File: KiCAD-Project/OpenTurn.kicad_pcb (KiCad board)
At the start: 4 copper layers, 66 x 84.5 mm, 146 parts, among them J201 XT30, J202 Conn_02x04_Odd_Even, J203 Conn_01x03_Shielded, J204 Conn_01x03_Shielded, J301 GPIOs, J302 JTAG/SWD, J303 Conn_01x03_Shielded, Q501 IAUC120N06S5N017ATMA1, Q502 IAUC120N06S5N017ATMA1, Q601 IAUC120N06S5N017ATMA1, Q602 IAUC120N06S5N017ATMA1, Q701 IAUC120N06S5N017ATMA1, Q702 IAUC120N06S5N017ATMA1, U201 TI_TCAN337G, U202 TLE5012B_E1000, U203 MAX15062A, U301 CY8C6244AZI-S4D92, U302 MCP9700AT-HTT, U401 DRV8323SRTAR-DRV8323SRTAR, Y301 32MHz

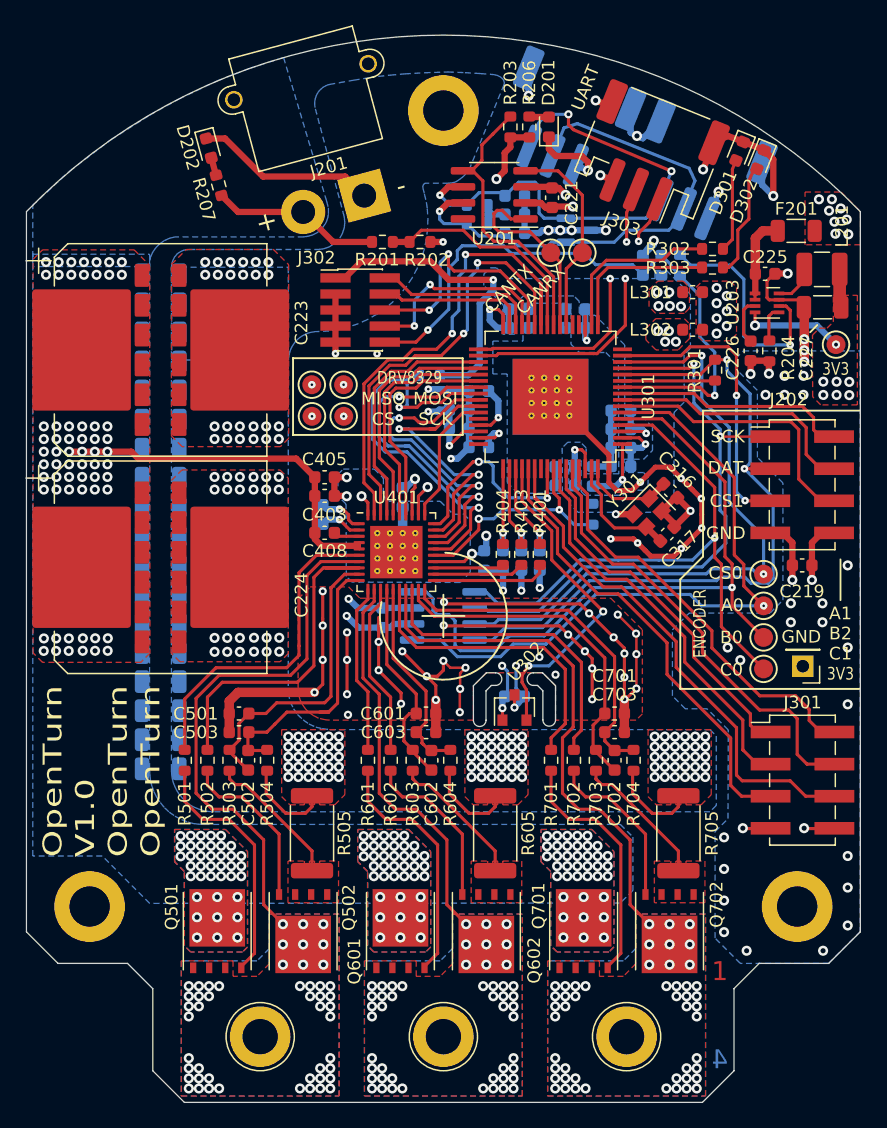
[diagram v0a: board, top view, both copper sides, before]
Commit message: changed connectors to THT
changed connectors to THT, removed UART connector
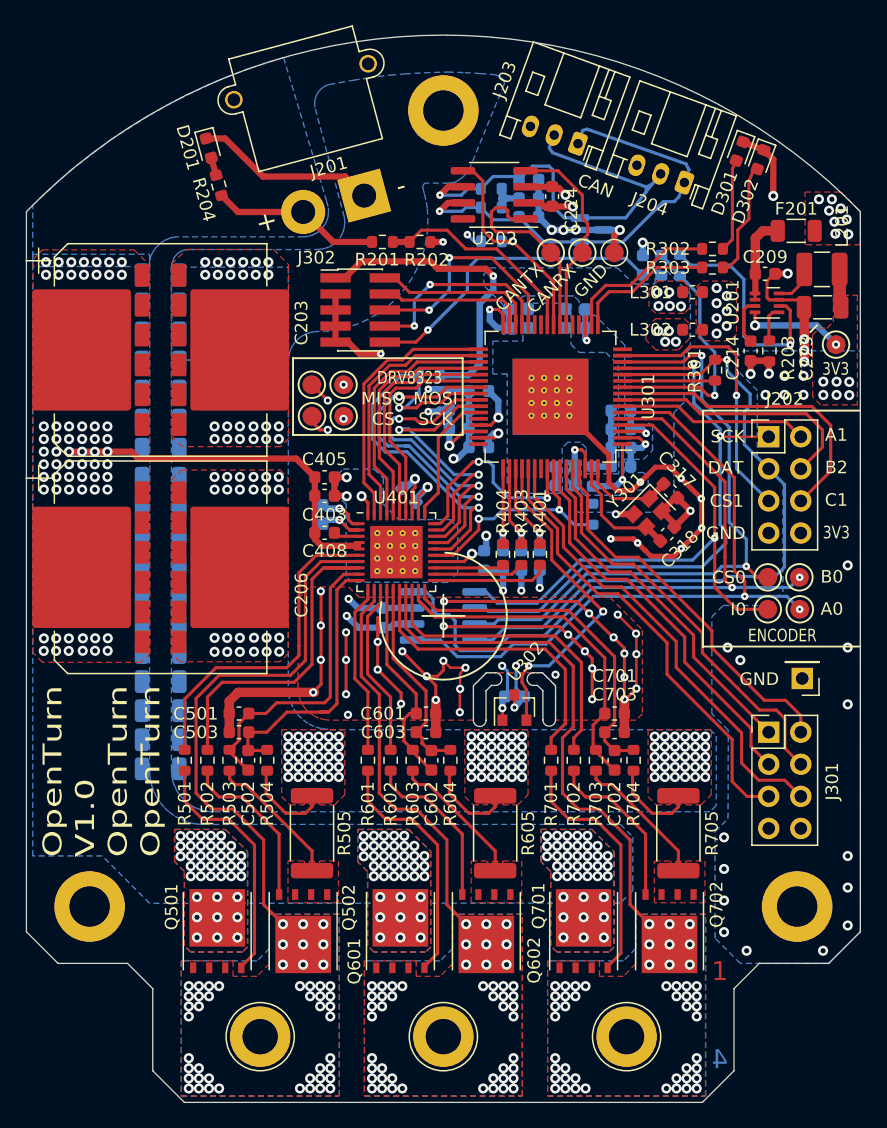
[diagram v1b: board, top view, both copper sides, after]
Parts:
- removed the C219 at (155.4, 123.0)
- removed the D201 at (135.3, 88.3)
- removed J303: Conn_01x03_Shielded, Connector_JST:JST_PH_S3B-PH-SM4-TB_1x03-1MP_P2.00mm_Horizontal
- removed the R206 at (133.8, 88.3)
- added TP203: CAN_GND, TestPoint:TestPoint_Pad_D1.5mm, F.Cu at (140.5, 98.2)
- C225: renamed from C1; value 100n -> 4n7
- J202, J301: footprint Connector_PinHeader_2.54mm:PinHeader_2x04_P2.54mm_Vertical_SMD -> Connector_PinHeader_2.54mm:PinHeader_2x04_P2.54mm_Vertical
- J203, J204: footprint Connector_JST:JST_PH_S3B-PH-SM4-TB_1x03-1MP_P2.00mm_Horizontal -> Connector_JST:JST_PH_S3B-PH-K_1x03_P2.00mm_Horizontal; moved to F.Cu
- R206: renamed from R203; moved to B.Cu
- moved R206 9.17 mm to (130.8, 97.3), turned to 0 degrees
- moved TP206 5.54 mm to (155.2, 123.9)
- moved TP204 4.73 mm to (152.7, 126.5), turned to 90 degrees
- moved J301 4.64 mm to (152.8, 136.2)
- moved J202 4.63 mm to (152.8, 112.8)
- moved TP207 2.88 mm to (155.2, 126.5), turned to 90 degrees
- moved J203 1.93 mm to (137.7, 89.6), turned to 160 degrees
- moved R207 1.69 mm to (130.8, 94.7)
- moved C226 1.69 mm to (133.8, 95.4)
- moved C227 1.69 mm to (133.8, 92.5)
- moved C225 1.69 mm to (133.8, 93.9)
- moved R208 1.69 mm to (130.8, 93.2)
- moved J204 1.16 mm to (146.1, 92.7), turned to 160 degrees
- moved D202 1.11 mm to (138.7, 96.4)
- moved TP302 0.98 mm to (155.4, 131.9)
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- renumbered C223 to C203, C203 to C204, C204 to C205, C224 to C206, C205 to C207, C206 to C208, C225 to C209, C207 to C210, C208 to C211, C209 to C212, C210 to C213, C226 to C214, C211 to C215, C212 to C216, C213 to C217, C214 to C218, C215 to C219, C216 to C220, C217 to C221, C218 to C222, C227 to C223, C221 to C224, C2 to C226, C3 to C227, C222 to C228, C311 to C305, C305 to C306, C322 to C307, C312 to C308, C306 to C309, C307 to C310, C314 to C311, C308 to C312, C309 to C313, C310 to C314, C313 to C315, C315 to C316, C316 to C317, C317 to C318, C318 to C319, D202 to D201, D1 to D202, R204 to R203, R207 to R204, R1 to R207, R2 to R208, R305 to R304, TP202 to TP201, TP203 to TP202, TP206 to TP204, TP204 to TP205, TP205 to TP206, TP201 to TP207, U203 to U201, U201 to U202, U202 to U203
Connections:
- C226 pad 1: Net-(C2-Pad1) -> Net-(C226-Pad1)
- C227 pad 1: Net-(C3-Pad1) -> Net-(C227-Pad1)
- D202 pad 1: Net-(C2-Pad1) -> Net-(C226-Pad1)
- D202 pad 2: Net-(C3-Pad1) -> Net-(C227-Pad1)
- H101 pad 1: GND -> unconnected-(H101-Pad1)
- H102 pad 1: GND -> unconnected-(H102-Pad1)
- J202 pad 2: /Interfaces/ENCODER_QOAD_I2 -> /Interfaces/ENCODER_QOAD_A2
- J202 pad 6: /Interfaces/ENCODER_QOAD_A2 -> /Interfaces/ENCODER_QOAD_I2
- J202 pad 7: GND -> +3V3
- J202 pad 8: +3V3 -> GND
- J203 pad 1: Net-(C3-Pad1) -> Net-(C226-Pad1)
- J203 pad 2: Net-(C2-Pad1) -> Net-(C227-Pad1)
- J204 pad 1: Net-(C3-Pad1) -> Net-(C226-Pad1)
- J204 pad 2: Net-(C2-Pad1) -> Net-(C227-Pad1)
- R207 pad 1: Net-(C2-Pad1) -> Net-(C226-Pad1)
- R208 pad 1: Net-(C3-Pad1) -> Net-(C227-Pad1)
- U202 pad 6: Net-(C3-Pad1) -> Net-(C227-Pad1)
- U202 pad 7: Net-(C2-Pad1) -> Net-(C226-Pad1)
- U301 pad 26: /MCU/DRV_PWM_AL -> unconnected-(U301-Pad26)
- U301 pad 27: /MCU/DRV_PWM_AH -> unconnected-(U301-Pad27)
- U301 pad 33: /MCU/DEBUG_UART_RX -> /MCU/DRV_PWM_AL
- U301 pad 34: /MCU/DEBUG_UART_TX -> /MCU/DRV_PWM_AH
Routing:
- net Net-(C2-Pad1): track 41.1 -> 0.00 mm, vias 1 -> 0
- net Net-(C3-Pad1): track 40.9 -> 0.00 mm, vias 3 -> 0
- net Net-(C226-Pad1): track 0.00 -> 36.6 mm, vias 0 -> 1
- net Net-(C227-Pad1): track 0.00 -> 36.1 mm, vias 0 -> 1
- net GND: track 307.9 -> 276.5 mm, vias 242 -> 227
- net /MCU/DEBUG_UART_TX: track 23.6 -> 0.00 mm, vias 2 -> 0
- net /MCU/DEBUG_UART_RX: track 22.9 -> 0.00 mm, vias 2 -> 0
- net /MCU/DRV_PWM_AL: track 39.4 -> 20.9 mm, vias 2 -> 0
- net /MCU/DRV_PWM_AH: track 33.9 -> 20.3 mm, vias 2 -> 0
- net +3V3: track 65.2 -> 56.8 mm, vias 20 -> 18
- net /Interfaces/ENCODER_QOAD_A2: track 22.1 -> 15.1 mm
- net /Interfaces/ENCODER_QOAD_I2: track 18.7 -> 24.5 mm
- net /Interfaces/CANFD_Fault: track 23.7 -> 18.1 mm, vias 0 -> 1
- net /MCU/GPIO5: track 41.0 -> 37.6 mm
- net /Interfaces/ENCODER_QOAD_I1: track 46.8 -> 43.8 mm
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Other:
- board text added: "48V 15A"
- board text added: "DRV8323"
- board text added: "I0"
- board text removed: "48V 20A"
- board text removed: "C0"
- board text removed: "DRV8329"
- board text removed: "UART"

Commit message: minor pcb updates
swapped Encoder Quadrature signals, to provide debug UART
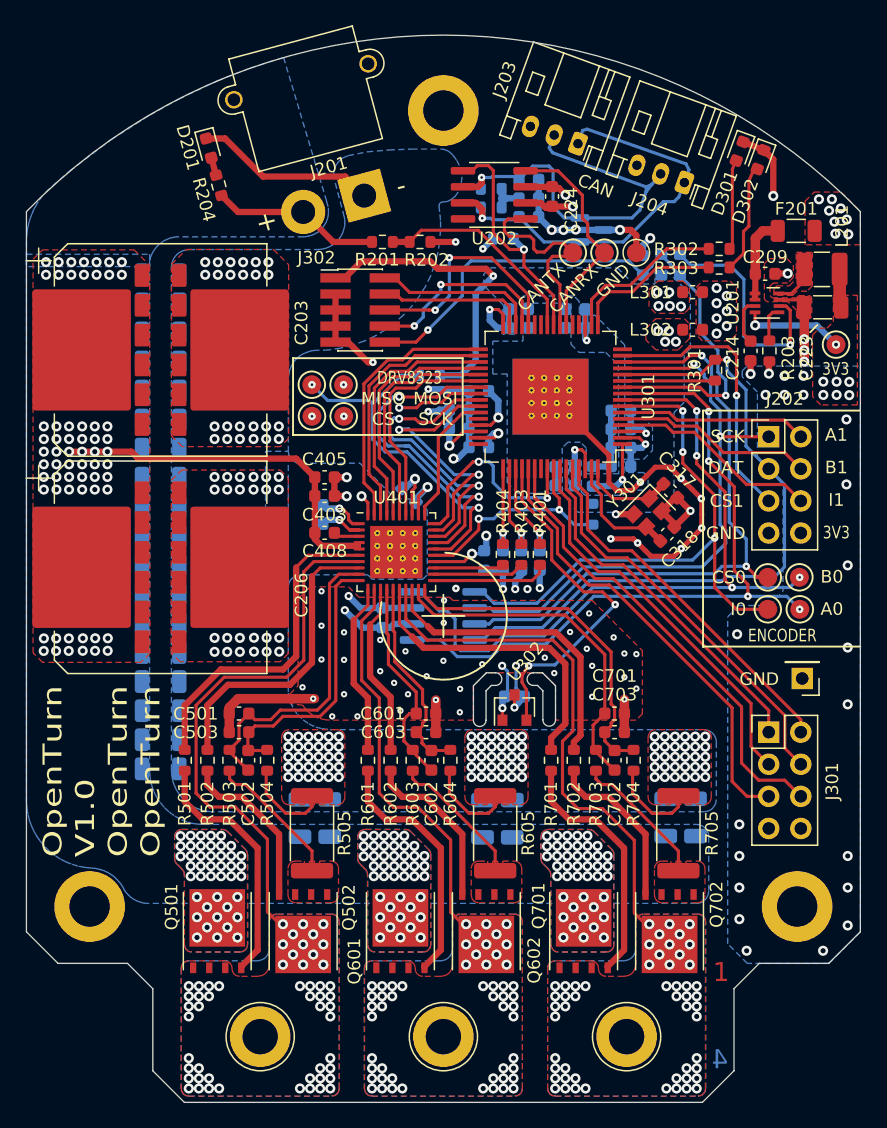
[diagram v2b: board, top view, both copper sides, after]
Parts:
- added C229: 10u, Capacitor_SMD:C_1206_3216Metric, B.Cu at (115.7, 143.0)
- added C230: 10u, Capacitor_SMD:C_1206_3216Metric, B.Cu at (132.4, 143.1)
- added C231: 10u, Capacitor_SMD:C_1206_3216Metric, B.Cu at (146.9, 142.9)
- added C232: 10u, Capacitor_SMD:C_1206_3216Metric, B.Cu at (118.0, 143.0)
- added C233: 10u, Capacitor_SMD:C_1206_3216Metric, B.Cu at (144.6, 142.9)
- added C234: 10u, Capacitor_SMD:C_1206_3216Metric, B.Cu at (130.1, 143.1)
- moved TP201 1.74 mm to (137.2, 98.2)
- moved TP202 1.74 mm to (139.7, 98.2)
- moved TP203 1.74 mm to (142.3, 98.2)
- moved R206 0.97 mm to (131.8, 97.2)
- moved R302 0.52 mm to (148.8, 98.0)
- moved R303 0.52 mm to (148.8, 99.4)
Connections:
- net /Power/Sheet61668C54/I_SENSE_N renamed /Power/ASNS_N
- net /Power/Sheet61668C54/I_SENSE_P renamed /Power/ASNS_P
- net /Power/sheet617091A8/I_SENSE_N renamed /Power/BSNS_N
- net /Power/sheet617091A8/I_SENSE_P renamed /Power/BSNS_P
- net /Power/sheet6171E233/I_SENSE_N renamed /Power/CSNS_N
- net /Power/sheet6171E233/I_SENSE_P renamed /Power/CSNS_P
- C228 pad 1: +3V3 -> VDDA
- U203 pad 6: +3V3 -> VDDA
- U301 pad 4: /Interfaces/ENCODER_QOAD_I1 -> /Interfaces/ENCODER_QOAD_I2
- U301 pad 5: /Interfaces/ENCODER_QOAD_B1 -> /Interfaces/ENCODER_QOAD_B2
- U301 pad 6: /Interfaces/ENCODER_QOAD_A1 -> /Interfaces/ENCODER_QOAD_A2
- U301 pad 7: /Interfaces/ENCODER_QOAD_A2 -> /Interfaces/ENCODER_QOAD_I1
- U301 pad 8: /Interfaces/ENCODER_QOAD_B2 -> /Interfaces/ENCODER_QOAD_B1
- U301 pad 9: /Interfaces/ENCODER_QOAD_I2 -> /Interfaces/ENCODER_QOAD_A1
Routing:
- net GND: track 276.5 -> 186.9 mm, vias 227 -> 233
- net +3V3: track 56.8 -> 15.7 mm, vias 18 -> 17
- net VDDA: track 17.9 -> 41.6 mm, vias 10 -> 11
- net /Interfaces/ENCODER_QOAD_I2: track 24.5 -> 16.6 mm
- net /Interfaces/ENCODER_QOAD_B2: track 20.6 -> 15.8 mm
- net /Power/Sheet61668C54/FET_GL: track 27.2 -> 24.1 mm
- net /Interfaces/ENCODER_QOAD_A1: track 54.3 -> 57.1 mm, vias 2 -> 4
- net Net-(C227-Pad1): track 36.1 -> 33.4 mm
- net /Interfaces/ENCODER_QOAD_I1: track 43.8 -> 46.5 mm, vias 1 -> 3
- net Net-(C226-Pad1): track 36.6 -> 33.9 mm
- net /Interfaces/ENCODER_QOAD_B1: track 55.5 -> 57.6 mm, vias 2 -> 4
- net /MCU/DRV_MISO: track 41.8 -> 43.7 mm
- net /MCU/TEMP1: track 26.2 -> 28.1 mm
- net /Power/CSNS_P: track 29.2 -> 27.6 mm
- net Net-(C209-Pad1): track 8.53 -> 6.93 mm
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- added copper zone on F.Cu, net Net-(L201-Pad1)
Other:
- board text added: "B1"
- board text added: "I1"
- board text removed: "B2"
- board text removed: "C1"
